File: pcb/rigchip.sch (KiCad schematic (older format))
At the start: 36 parts, among them IC1 TSR1, IC2 CHIPv1_0, IC3 SN74LVC1G07, IC4 SN74LVC1G07, J1 POWER, J2 DATA, J3 CONTROL, X1 CONN, X2 CONN

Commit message: add part number for smps
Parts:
- IC1: Farnell (none) -> 1696320
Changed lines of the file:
@@
 F 2 "agg:TSR1" H 2350 700 50  0001 L CNN
 F 3 "http://www.tracopower.com/products/tsr1.pdf" H 2350 600 50  0001 L CNN
+F 4 "1696320" H 2650 1000 60  0001 C CNN "Farnell"
 	1    2650 1000
 	1    0    0    -1

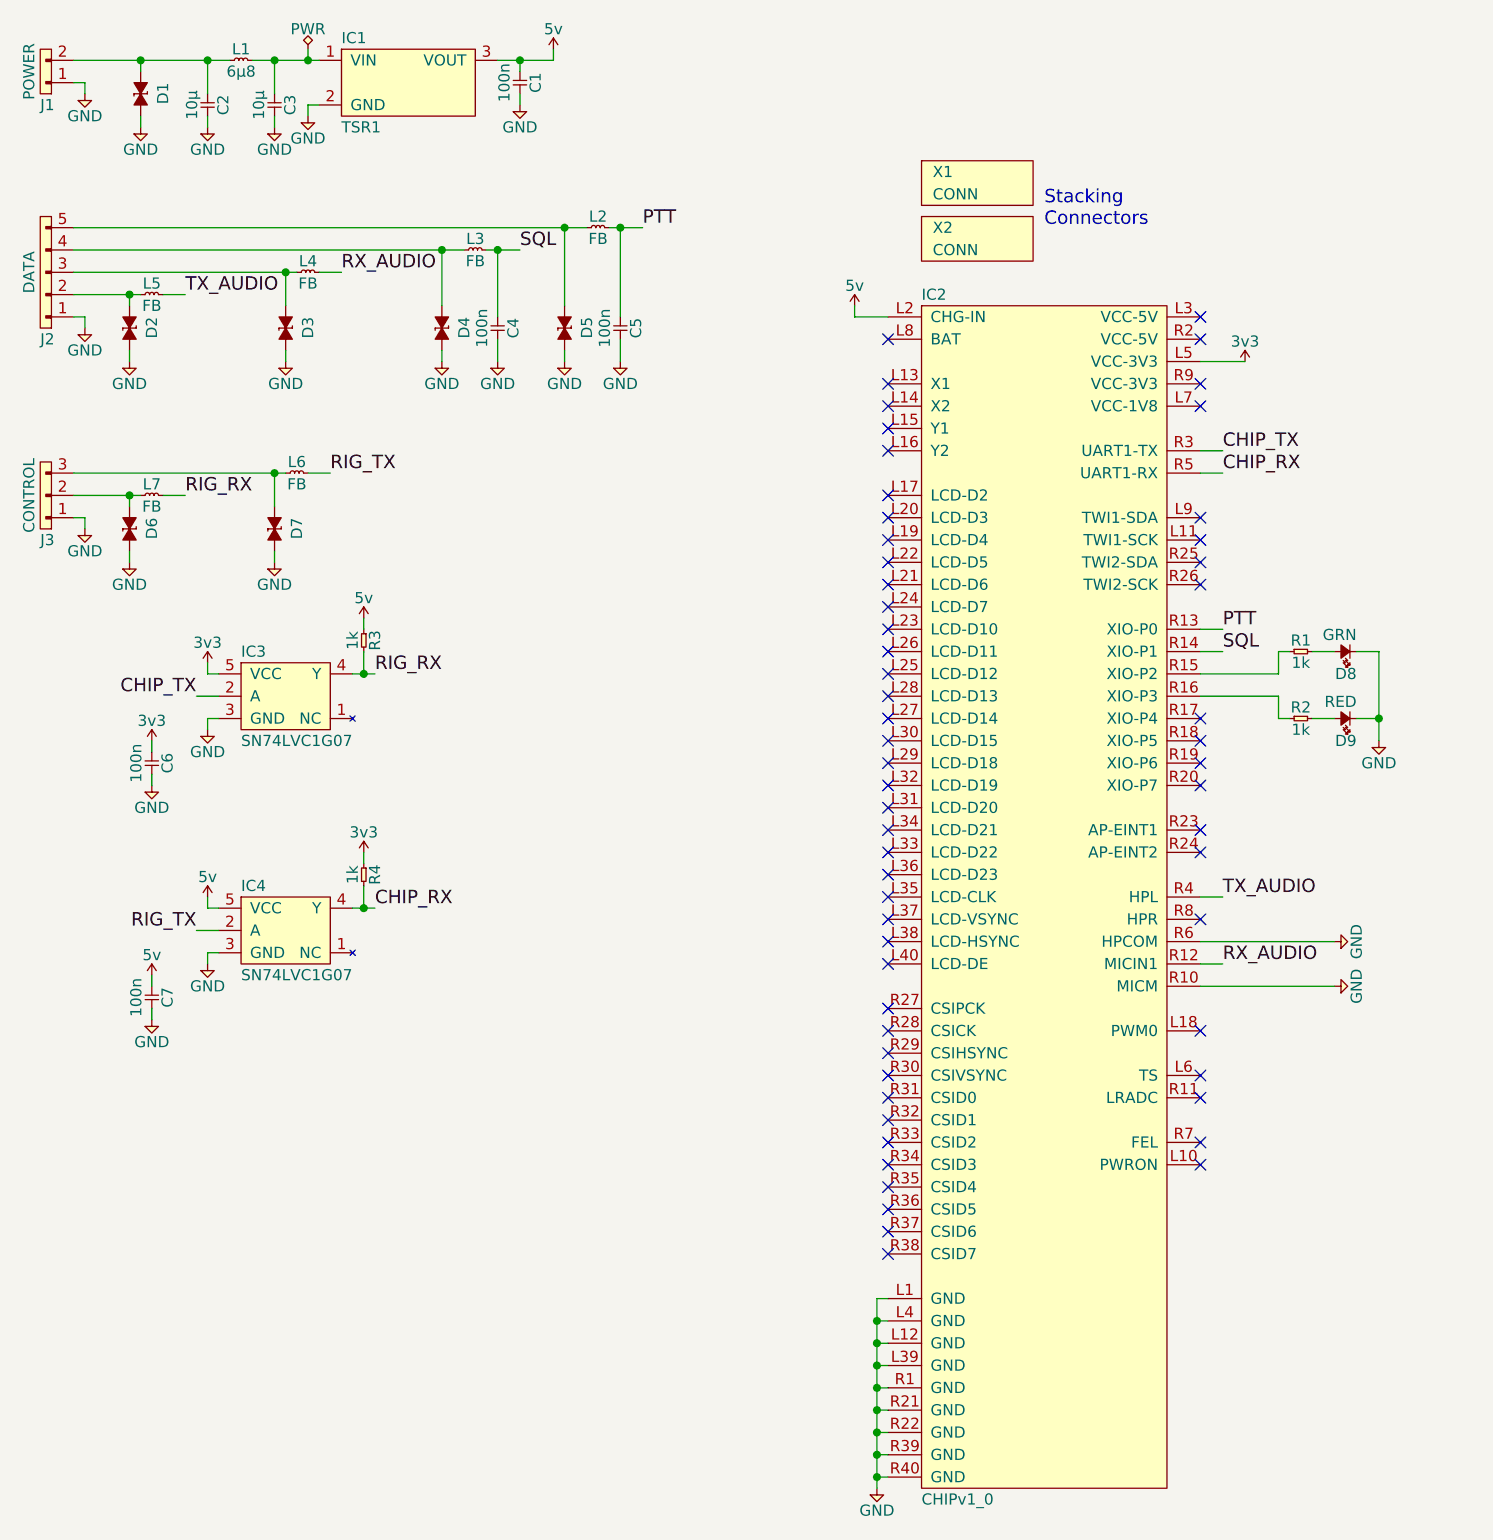
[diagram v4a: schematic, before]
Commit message: LEDs to sink, driver on PTT, zener+R on SQL, reroute
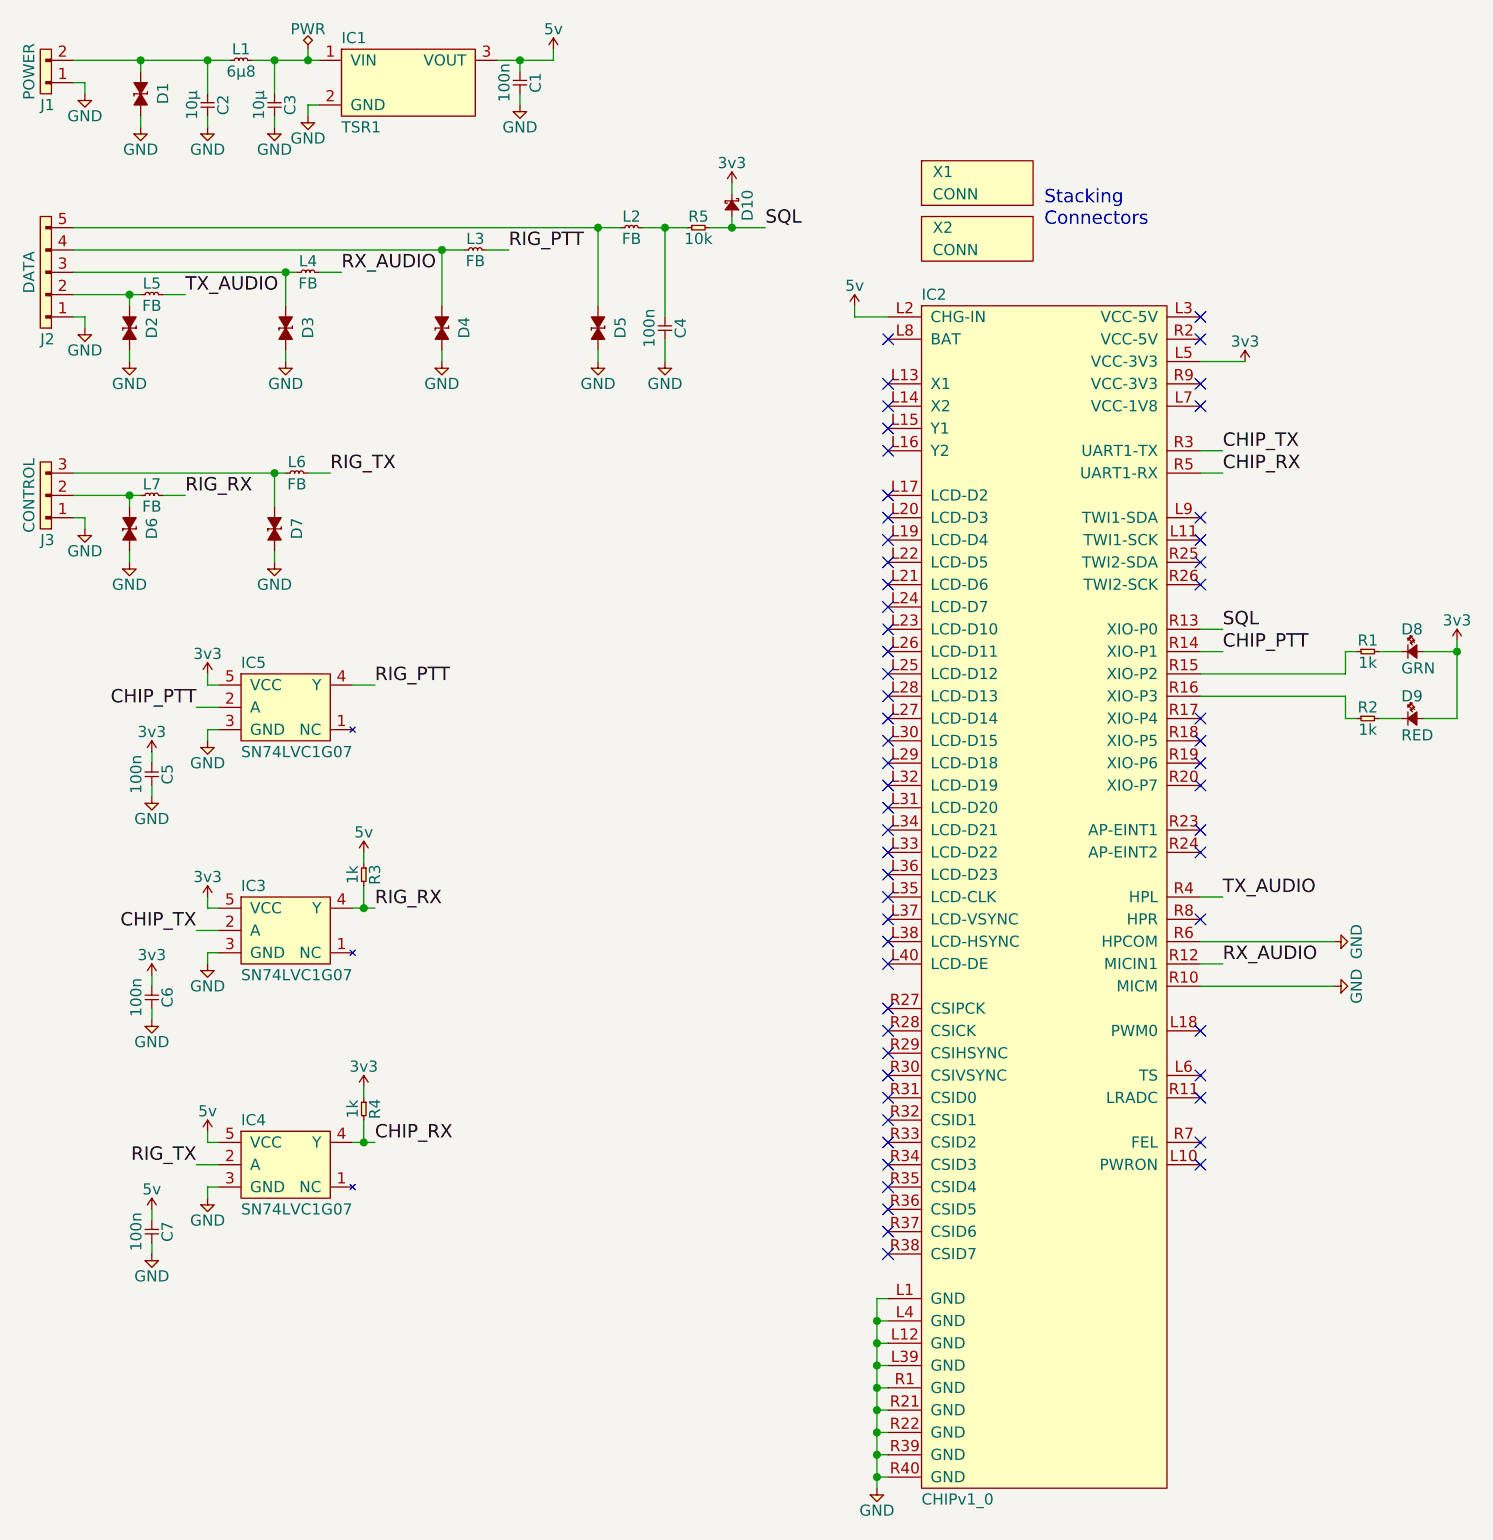
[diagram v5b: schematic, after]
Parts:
- added D10: ~, agg:0603-LED, symbol SCHOTTKY
- added IC5: SN74LVC1G07, agg:SOT-23-5, symbol SN74LVC1G07
- added R5: 10k, agg:0603, symbol R
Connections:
- net 3v3: now also C5.1, D8.2, D9.2, D10.1, IC5.5 (VCC)
- net GND: now also IC5.3 (GND); no longer D8.1, D9.1
- net SQL: now also IC2.R13 (XIO-P0), D10.2, R5.2; no longer C4.1, IC2.R14 (XIO-P1), L3.2
- net at R1.2: now also D8.1; no longer D8.2
- net at R2.2: now also D9.1; no longer D9.2
- removed net PTT: C5.1, IC2.R13 (XIO-P0), L2.2
- new net: C4.1, L2.2, R5.1
- new net CHIP_PTT: IC2.R14 (XIO-P1), IC5.2 (A)
- new net RIG_PTT: IC5.4 (Y), L3.2
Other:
- moved on the sheet: C4, C6, C7, D5, D8, D9, IC3, IC4, L2, R1, R2, R3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

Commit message: add farnell #s
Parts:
- C1, C4, C5, C6, C7: Farnell (none) -> 2496834
- C2, C3: Farnell (none) -> 2211092
- D10: Farnell (none) -> 2341897
- D8: Farnell (none) -> 2290328
- D9: Farnell (none) -> 2290329
- J1: Farnell (none) -> 1830747
- J2: Farnell (none) -> 1830750
- J3: Farnell (none) -> 1830748
- L2, L3, L4, L5, L6, L7: Farnell (none) -> 1463451
- R1, R2, R3, R4: Farnell (none) -> 9238484
- R5: Farnell (none) -> 9238603
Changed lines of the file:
@@
 F 2 "agg:S05B-PASK-2" H 1050 2050 50  0001 C CNN
 F 3 "" H 1050 2050 50  0001 C CNN
+F 4 "1830750" H 1050 2050 60  0001 C CNN "Farnell"
 	1    1050 2050
 	1    0    0    1
@@
 F 2 "agg:S03B-PASK-2" H 1050 2950 50  0001 C CNN
 F 3 "" H 1050 2950 50  0001 C CNN
+F 4 "1830748" H 1050 2950 60  0001 C CNN "Farnell"
 	1    1050 2950
 	1    0    0    1
@@
 F 2 "agg:S02B-PASK-2" H 1050 1000 50  0001 C CNN
 F 3 "" H 1050 1000 50  0001 C CNN
+F 4 "1830747" H 1050 1000 60  0001 C CNN "Farnell"
 	1    1050 1000
 	1    0    0    1
@@
 F 2 "agg:1206" H 1750 1050 50  0001 C CNN
 F 3 "" H 1750 1050 50  0001 C CNN
+F 4 "2211092" H 1750 1050 60  0001 C CNN "Farnell"
 	1    1750 1050
 	0    1    1    0
@@
 F 2 "agg:1206" H 2050 1050 50  0001 C CNN
 F 3 "" H 2050 1050 50  0001 C CNN
+F 4 "2211092" H 2050 1050 60  0001 C CNN "Farnell"
 	1    2050 1050
 	0    1    1    0
@@
 F 2 "agg:0603" H 1450 1950 50  0001 C CNN
 F 3 "" H 1450 1950 50  0001 C CNN
+F 4 "1463451" H 1450 1950 60  0001 C CNN "Farnell"
 	1    1450 1950
 	1    0    0    -1
@@
 F 2 "agg:0603" H 3800 2050 50  0001 C CNN
 F 3 "" H 3800 2050 50  0001 C CNN
+F 4 "2496834" H 3800 2050 60  0001 C CNN "Farnell"
 	1    3800 2050
 	0    1    1    0
@@
 F 2 "agg:0603" H 3150 950 50  0001 C CNN
 F 3 "" H 3150 950 50  0001 C CNN
+F 4 "2496834" H 3150 950 60  0001 C CNN "Farnell"
 	1    3150 950
 	0    1    1    0
@@
 F 2 "agg:0603" H 2150 1850 50  0001 C CNN
 F 3 "" H 2150 1850 50  0001 C CNN
+F 4 "1463451" H 2150 1850 60  0001 C CNN "Farnell"
 	1    2150 1850
 	1    0    0    -1
@@
 F 2 "agg:0603" H 2900 1750 50  0001 C CNN
 F 3 "" H 2900 1750 50  0001 C CNN
+F 4 "1463451" H 2900 1750 60  0001 C CNN "Farnell"
 	1    2900 1750
 	1    0    0    -1
@@
 F 2 "agg:0603" H 3600 1650 50  0001 C CNN
 F 3 "" H 3600 1650 50  0001 C CNN
+F 4 "1463451" H 3600 1650 60  0001 C CNN "Farnell"
 	1    3600 1650
 	1    0    0    -1
@@
 F 2 "agg:0603" H 1450 2850 50  0001 C CNN
 F 3 "" H 1450 2850 50  0001 C CNN
+F 4 "1463451" H 1450 2850 60  0001 C CNN "Farnell"
 	1    1450 2850
 	1    0    0    -1
@@
 F 2 "agg:0603" H 2100 2750 50  0001 C CNN
 F 3 "" H 2100 2750 50  0001 C CNN
+F 4 "1463451" H 2100 2750 60  0001 C CNN "Farnell"
 	1    2100 2750
 	1    0    0    -1
@@
 F 2 "agg:0603-LED" H 7100 3550 50  0001 C CNN
 F 3 "" H 7100 3550 50  0001 C CNN
+F 4 "2290328" H 7100 3550 60  0001 C CNN "Farnell"
 	1    7100 3550
 	1    0    0    -1
@@
 F 2 "agg:0603-LED" H 7100 3850 50  0001 C CNN
 F 3 "" H 7100 3850 50  0001 C CNN
+F 4 "2290329" H 7100 3850 60  0001 C CNN "Farnell"
 	1    7100 3850
 	1    0    0    -1
@@
 F 2 "agg:0603" H 6900 3550 50  0001 C CNN
 F 3 "" H 6900 3550 50  0001 C CNN
+F 4 "9238484" H 6900 3550 60  0001 C CNN "Farnell"
 	1    6900 3550
 	1    0    0    -1
@@
 F 2 "agg:0603" H 6900 3850 50  0001 C CNN
 F 3 "" H 6900 3850 50  0001 C CNN
+F 4 "9238484" H 6900 3850 60  0001 C CNN "Farnell"
 	1    6900 3850
 	1    0    0    -1
@@
 F 2 "agg:0603" H 1500 5050 50  0001 C CNN
 F 3 "" H 1500 5050 50  0001 C CNN
+F 4 "2496834" H 1500 5050 60  0001 C CNN "Farnell"
 	1    1500 5050
 	0    1    1    0
@@
 F 2 "agg:0603" H 2450 4500 50  0001 C CNN
 F 3 "" H 2450 4500 50  0001 C CNN
+F 4 "9238484" H 2450 4500 60  0001 C CNN "Farnell"
 	1    2450 4500
 	0    1    1    0
@@
 F 2 "agg:0603" H 2450 5550 50  0001 C CNN
 F 3 "" H 2450 5550 50  0001 C CNN
+F 4 "9238484" H 2450 5550 60  0001 C CNN "Farnell"
 	1    2450 5550
 	0    1    1    0
@@
 F 2 "agg:0603" H 1500 6100 50  0001 C CNN
 F 3 "" H 1500 6100 50  0001 C CNN
+F 4 "2496834" H 1500 6100 60  0001 C CNN "Farnell"
 	1    1500 6100
 	0    1    1    0
@@
 F 2 "agg:0603" H 1500 4050 50  0001 C CNN
 F 3 "" H 1500 4050 50  0001 C CNN
+F 4 "2496834" H 1500 4050 60  0001 C CNN "Farnell"
 	1    1500 4050
 	0    1    1    0
@@
 F 2 "agg:0603" H 3900 1650 50  0001 C CNN
 F 3 "" H 3900 1650 50  0001 C CNN
+F 4 "9238603" H 3900 1650 60  0001 C CNN "Farnell"
 	1    3900 1650
 	1    0    0    -1
@@
 F 2 "agg:0603-LED" H 4050 1470 50  0001 C CNN
 F 3 "" H 4150 1570 50  0001 C CNN
+F 4 "2341897" H 4100 1500 60  0001 C CNN "Farnell"
 	1    4100 1500
 	0    1    1    0
